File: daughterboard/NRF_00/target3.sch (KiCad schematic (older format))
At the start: 0 parts

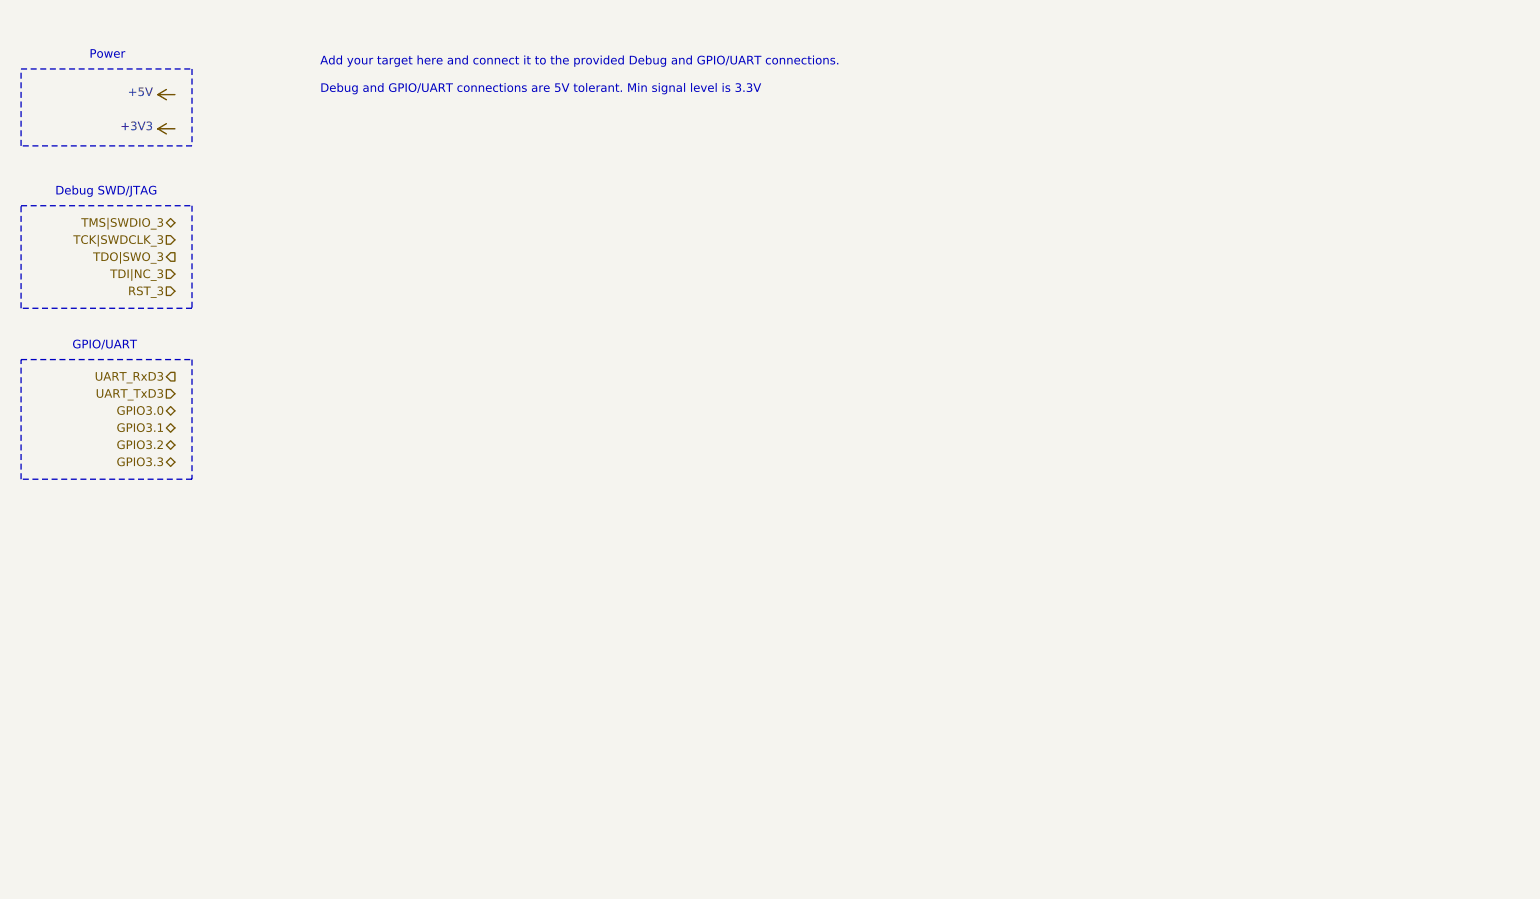
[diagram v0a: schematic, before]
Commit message: finished NRF daughterboard schematics
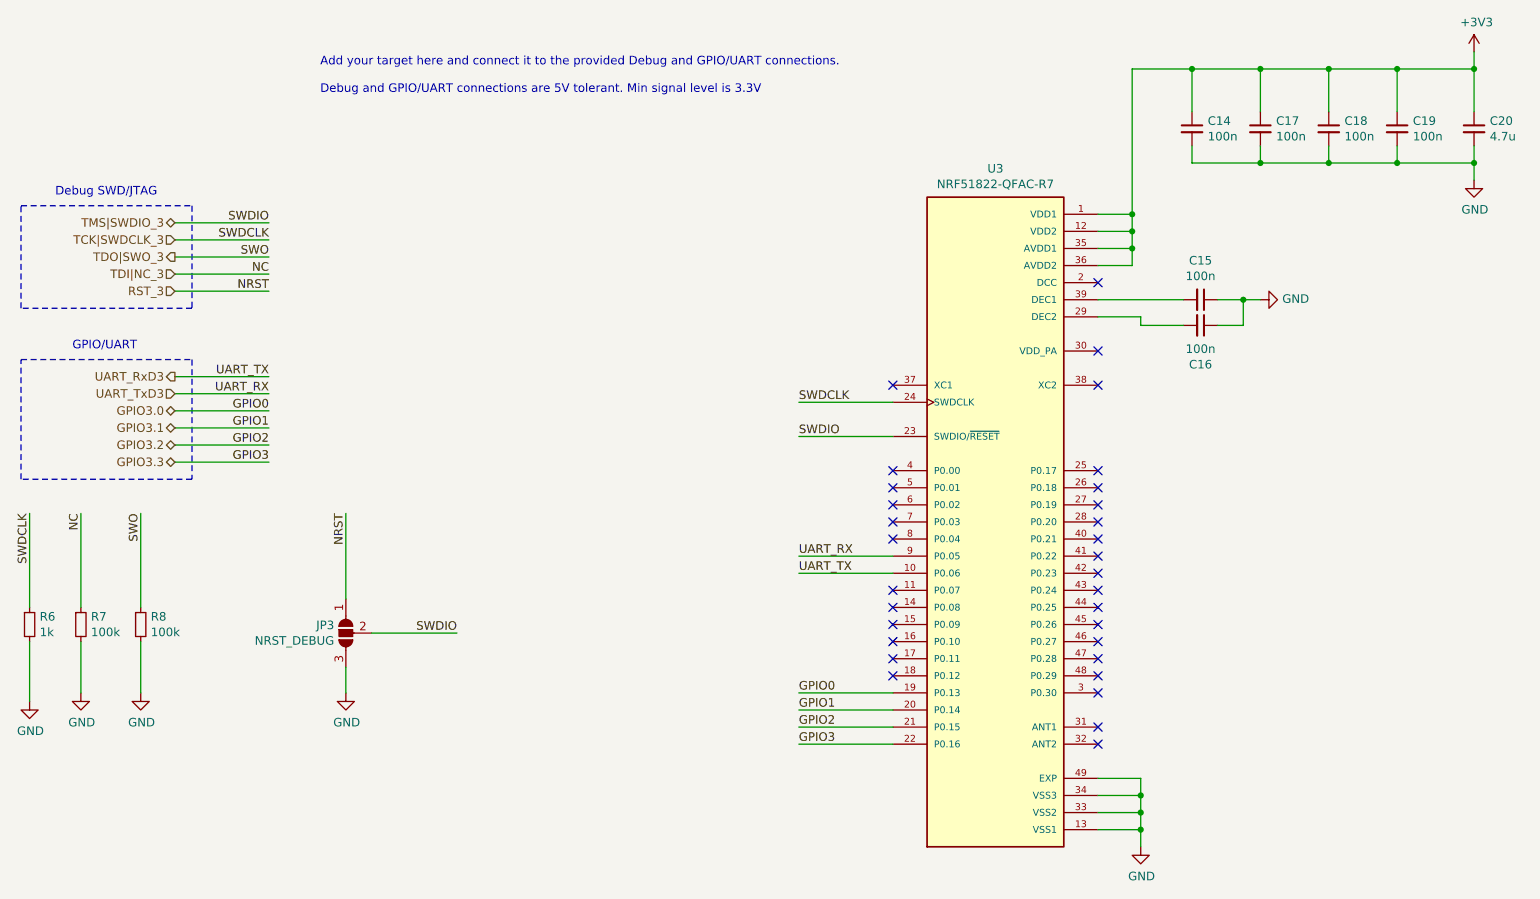
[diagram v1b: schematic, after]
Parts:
- added C14, C15, C16, C17, C18, C19: 100n, symbol Device:C_Small
- added C20: 4.7u, symbol Device:C_Small
- added JP3: NRST_DEBUG, symbol Jumper:SolderJumper_3_Open
- added R6: 1k, symbol Device:R_Small
- added R7, R8: 100k, symbol Device:R_Small
- added U3: NRF51822-QFAC-R7, hive_daughterboard:NRF51822-QFAC-R7, symbol hive_daughterboard:NRF51822-QFAC-R7
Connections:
- net +3V3: now also C14.1, C17.1, C18.1, C19.1, C20.1, U3.1 (VDD1), U3.12 (VDD2), U3.35 (AVDD1), U3.36 (AVDD2)
- net GPIO3.0: now also U3.19 (P0.13)
- net GPIO3.1: now also U3.20 (P0.14)
- net GPIO3.2: now also U3.21 (P0.15)
- net GPIO3.3: now also U3.22 (P0.16)
- net RST_3: now also JP3.1 (A)
- net TCK|SWDCLK_3: now also R6.1, U3.24 (SWDCLK)
- net TDI|NC_3: now also R7.1
- net TDO|SWO_3: now also R8.1
- net TMS|SWDIO_3: now also JP3.2 (C), U3.23 (SWDIO/~RESET)
- net UART_RxD3: now also U3.10 (P0.06)
- net UART_TxD3: now also U3.9 (P0.05)
- new net: C16.2, U3.29 (DEC2)
- new net: C15.2, U3.39 (DEC1)
- new net GND: C14.2, C15.1, C16.1, C17.2, C18.2, C19.2, C20.2, JP3.3 (B), R6.2, R7.2, R8.2, U3.13 (VSS1), U3.33 (VSS2), U3.34 (VSS3), U3.49 (EXP)
- no-connect marks 0 -> 31
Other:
- note removed: "Power"

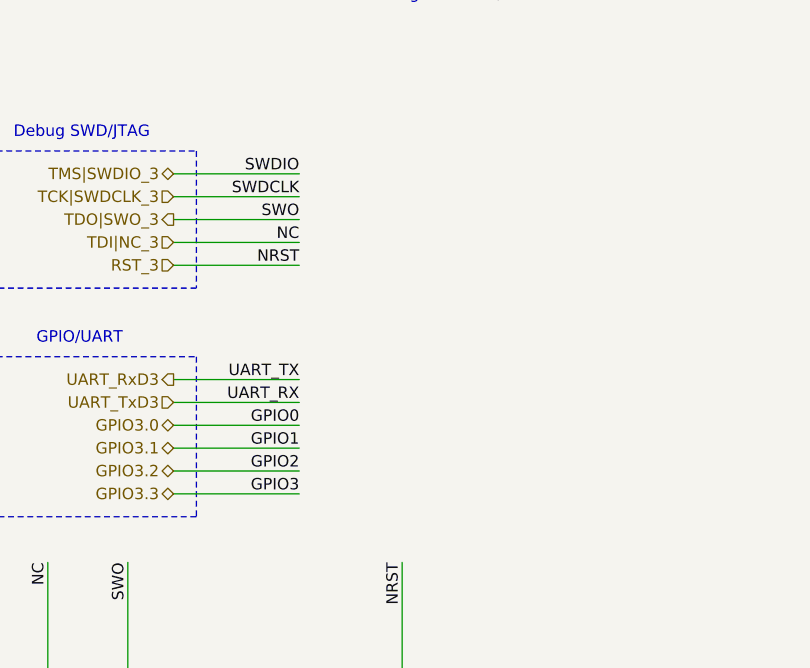
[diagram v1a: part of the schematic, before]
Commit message: added testpoints to daughterboards, updated readme
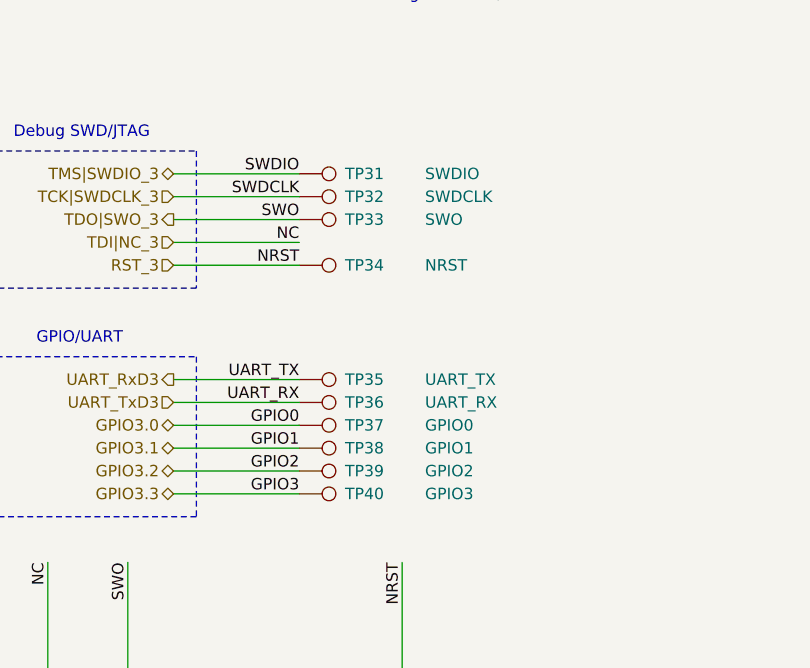
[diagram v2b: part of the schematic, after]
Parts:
- added TP31: SWDIO, symbol Connector:TestPoint
- added TP32: SWDCLK, symbol Connector:TestPoint
- added TP33: SWO, symbol Connector:TestPoint
- added TP34: NRST, symbol Connector:TestPoint
- added TP35: UART_TX, symbol Connector:TestPoint
- added TP36: UART_RX, symbol Connector:TestPoint
- added TP37: GPIO0, symbol Connector:TestPoint
- added TP38: GPIO1, symbol Connector:TestPoint
- added TP39: GPIO2, symbol Connector:TestPoint
- added TP40: GPIO3, symbol Connector:TestPoint
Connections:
- net GPIO3.0: now also TP37.1
- net GPIO3.1: now also TP38.1
- net GPIO3.2: now also TP39.1
- net GPIO3.3: now also TP40.1
- net RST_3: now also TP34.1
- net TCK|SWDCLK_3: now also TP32.1
- net TDO|SWO_3: now also TP33.1
- net TMS|SWDIO_3: now also TP31.1
- net UART_RxD3: now also TP35.1
- net UART_TxD3: now also TP36.1
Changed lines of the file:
@@
 	7300 5350 7300 5250
 Connection ~ 7300 5250
+$Comp
+L Connector:TestPoint TP?
+U 1 1 61914E59
+P 2200 2100
+AR Path="/616688D6/61914E59" Ref="TP?"  Part="1"
+AR Path="/61668157/61914E59" Ref="TP34"  Part="1"
+F 0 "TP34" V 2200 2300 50  0000 L CNN
+F 1 "NRST" V 2200 2650 50  0000 L CNN
+F 2 "" H 2400 2100 50  0001 C CNN
+F 3 "~" H 2400 2100 50  0001 C CNN
+	1    2200 2100
+	0    1    1    0
+$EndComp
+$Comp
+L Connector:TestPoint TP?
+U 1 1 61914E5F
+P 2200 1900
+AR Path="/616688D6/61914E5F" Ref="TP?"  Part="1"
+AR Path="/61668157/61914E5F" Ref="TP33"  Part="1"
+F 0 "TP33" V 2200 2100 50  0000 L CNN
+F 1 "SWO" V 2200 2450 50  0000 L CNN
+F 2 "" H 2400 1900 50  0001 C CNN
+F 3 "~" H 2400 1900 50  0001 C CNN
+	1    2200 1900
+	0    1    1    0
+$EndComp
+$Comp
+L Connector:TestPoint TP?
+U 1 1 61914E65
+P 2200 1800
+AR Path="/616688D6/61914E65" Ref="TP?"  Part="1"
+AR Path="/61668157/61914E65" Ref="TP32"  Part="1"
+F 0 "TP32" V 2200 2000 50  0000 L CNN
+F 1 "SWDCLK" V 2200 2350 50  0000 L CNN
+F 2 "" H 2400 1800 50  0001 C CNN
+F 3 "~" H 2400 1800 50  0001 C CNN
+	1    2200 1800
+	0    1    1    0
+$EndComp
+$Comp
+L Connector:TestPoint TP?
+U 1 1 61914E6B
+P 2200 1700
+AR Path="/616688D6/61914E6B" Ref="TP?"  Part="1"
+AR Path="/61668157/61914E6B" Ref="TP31"  Part="1"
+F 0 "TP31" V 2200 1900 50  0000 L CNN
+F 1 "SWDIO" V 2200 2250 50  0000 L CNN
+F 2 "" H 2400 1700 50  0001 C CNN
+F 3 "~" H 2400 1700 50  0001 C CNN
+	1    2200 1700
+	0    1    1    0
+$EndComp
+$Comp
+L Connector:TestPoint TP?
+U 1 1 61914E71
+P 2200 2600
+AR Path="/616688D6/61914E71" Ref="TP?"  Part="1"
+AR Path="/61668157/61914E71" Ref="TP35"  Part="1"
+F 0 "TP35" V 2200 2800 50  0000 L CNN
+F 1 "UART_TX" V 2200 3150 50  0000 L CNN
+F 2 "" H 2400 2600 50  0001 C CNN
+F 3 "~" H 2400 2600 50  0001 C CNN
+	1    2200 2600
+	0    1    1    0
+$EndComp
+$Comp
+L Connector:TestPoint TP?
+U 1 1 61914E77
+P 2200 2700
+AR Path="/616688D6/61914E77" Ref="TP?"  Part="1"
+AR Path="/61668157/61914E77" Ref="TP36"  Part="1"
+F 0 "TP36" V 2200 2900 50  0000 L CNN
+F 1 "UART_RX" V 2200 3250 50  0000 L CNN
+F 2 "" H 2400 2700 50  0001 C CNN
+F 3 "~" H 2400 2700 50  0001 C CNN
+	1    2200 2700
+	0    1    1    0
+$EndComp
+$Comp
+L Connector:TestPoint TP?
+U 1 1 61914E7D
+P 2200 2800
+AR Path="/616688D6/61914E7D" Ref="TP?"  Part="1"
+AR Path="/61668157/61914E7D" Ref="TP37"  Part="1"
+F 0 "TP37" V 2200 3000 50  0000 L CNN
+F 1 "GPIO0" V 2200 3350 50  0000 L CNN
+F 2 "" H 2400 2800 50  0001 C CNN
+F 3 "~" H 2400 2800 50  0001 C CNN
+	1    2200 2800
+	0    1    1    0
+$EndComp
+$Comp
+L Connector:TestPoint TP?
+U 1 1 61914E83
+P 2200 2900
+AR Path="/616688D6/61914E83" Ref="TP?"  Part="1"
+AR Path="/61668157/61914E83" Ref="TP38"  Part="1"
+F 0 "TP38" V 2200 3100 50  0000 L CNN
+F 1 "GPIO1" V 2200 3450 50  0000 L CNN
+F 2 "" H 2400 2900 50  0001 C CNN
+F 3 "~" H 2400 2900 50  0001 C CNN
+	1    2200 2900
+	0    1    1    0
+$EndComp
+$Comp
+L Connector:TestPoint TP?
+U 1 1 61914E89
+P 2200 3000
+AR Path="/616688D6/61914E89" Ref="TP?"  Part="1"
+AR Path="/61668157/61914E89" Ref="TP39"  Part="1"
+F 0 "TP39" V 2200 3200 50  0000 L CNN
+F 1 "GPIO2" V 2200 3550 50  0000 L CNN
+F 2 "" H 2400 3000 50  0001 C CNN
+F 3 "~" H 2400 3000 50  0001 C CNN
+	1    2200 3000
+	0    1    1    0
+$EndComp
+$Comp
+L Connector:TestPoint TP?
+U 1 1 61914E8F
+P 2200 3100
+AR Path="/616688D6/61914E8F" Ref="TP?"  Part="1"
+AR Path="/61668157/61914E8F" Ref="TP40"  Part="1"
+F 0 "TP40" V 2200 3300 50  0000 L CNN
+F 1 "GPIO3" V 2200 3650 50  0000 L CNN
+F 2 "" H 2400 3100 50  0001 C CNN
+F 3 "~" H 2400 3100 50  0001 C CNN
+	1    2200 3100
+	0    1    1    0
+$EndComp
 $EndSCHEMATC

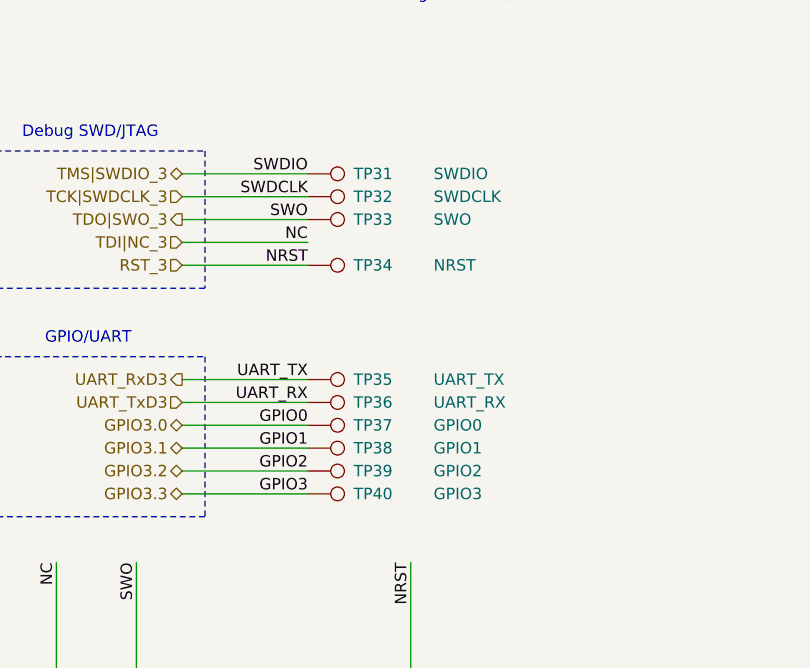
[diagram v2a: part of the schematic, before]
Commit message: finished NRF daughterboard layout
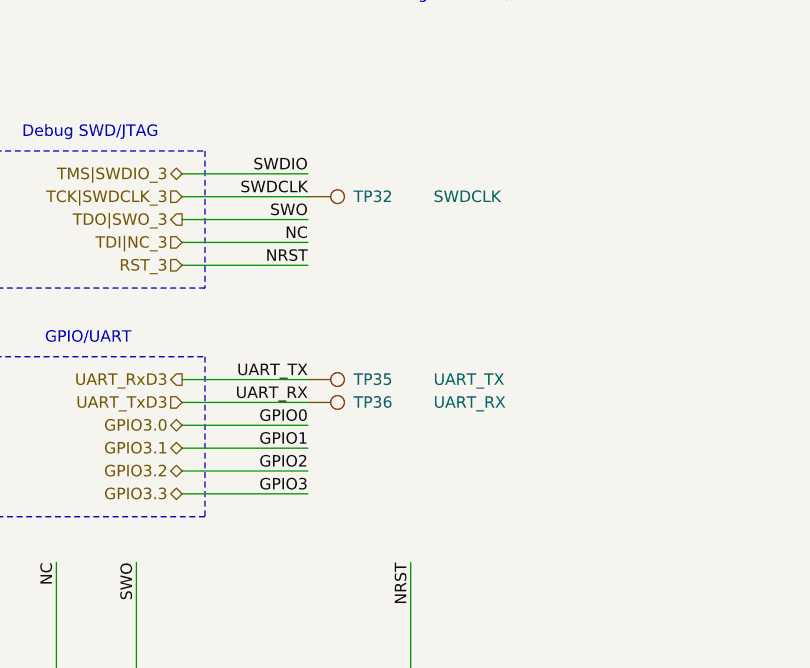
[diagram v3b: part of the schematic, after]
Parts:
- removed TP31: SWDIO, symbol Connector:TestPoint
- removed TP33: SWO, symbol Connector:TestPoint
- removed TP34: NRST, symbol Connector:TestPoint
- removed TP37: GPIO0, symbol Connector:TestPoint
- removed TP38: GPIO1, symbol Connector:TestPoint
- removed TP39: GPIO2, symbol Connector:TestPoint
- removed TP40: GPIO3, symbol Connector:TestPoint
- C14, C15, C16, C17, C18, C19, C20: footprint (none) -> Capacitor_SMD:C_0603_1608Metric_Pad1.05x0.95mm_HandSolder
- JP3: footprint (none) -> Jumper:SolderJumper-3_P2.0mm_Open_TrianglePad1.0x1.5mm_NumberLabels
- R6, R7, R8: footprint (none) -> Resistor_SMD:R_0603_1608Metric_Pad1.05x0.95mm_HandSolder
- TP32, TP35, TP36: footprint (none) -> TestPoint:TestPoint_Pad_1.0x1.0mm
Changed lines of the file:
@@
 F 0 "R7" H 1159 4096 50  0000 L CNN
 F 1 "100k" H 1159 4005 50  0000 L CNN
-F 2 "" H 1100 4050 50  0001 C CNN
+F 2 "Resistor_SMD:R_0603_1608Metric_Pad1.05x0.95mm_HandSolder" H 1100 4050 50  0001 C CNN
 F 3 "~" H 1100 4050 50  0001 C CNN
 	1    1100 4050
@@
 F 0 "R6" H 859 4096 50  0000 L CNN
 F 1 "1k" H 859 4005 50  0000 L CNN
-F 2 "" H 800 4050 50  0001 C CNN
+F 2 "Resistor_SMD:R_0603_1608Metric_Pad1.05x0.95mm_HandSolder" H 800 4050 50  0001 C CNN
 F 3 "~" H 800 4050 50  0001 C CNN
 	1    800  4050
@@
 F 0 "JP3" V 2604 4168 50  0000 L CNN
 F 1 "NRST_DEBUG" V 2695 4168 50  0000 L CNN
-F 2 "" H 2650 4100 50  0001 C CNN
+F 2 "Jumper:SolderJumper-3_P2.0mm_Open_TrianglePad1.0x1.5mm_NumberLabels" H 2650 4100 50  0001 C CNN
 F 3 "~" H 2650 4100 50  0001 C CNN
 	1    2650 4100
@@
 F 0 "C14" H 7692 1196 50  0000 L CNN
 F 1 "100n" H 7692 1105 50  0000 L CNN
-F 2 "" H 7600 1150 50  0001 C CNN
+F 2 "Capacitor_SMD:C_0603_1608Metric_Pad1.05x0.95mm_HandSolder" H 7600 1150 50  0001 C CNN
 F 3 "~" H 7600 1150 50  0001 C CNN
 	1    7600 1150
@@
 F 0 "C17" H 8092 1196 50  0000 L CNN
 F 1 "100n" H 8092 1105 50  0000 L CNN
-F 2 "" H 8000 1150 50  0001 C CNN
+F 2 "Capacitor_SMD:C_0603_1608Metric_Pad1.05x0.95mm_HandSolder" H 8000 1150 50  0001 C CNN
 F 3 "~" H 8000 1150 50  0001 C CNN
 	1    8000 1150
@@
 F 0 "C18" H 8492 1196 50  0000 L CNN
 F 1 "100n" H 8492 1105 50  0000 L CNN
-F 2 "" H 8400 1150 50  0001 C CNN
+F 2 "Capacitor_SMD:C_0603_1608Metric_Pad1.05x0.95mm_HandSolder" H 8400 1150 50  0001 C CNN
 F 3 "~" H 8400 1150 50  0001 C CNN
 	1    8400 1150
@@
 F 0 "C19" H 8892 1196 50  0000 L CNN
 F 1 "100n" H 8892 1105 50  0000 L CNN
-F 2 "" H 8800 1150 50  0001 C CNN
+F 2 "Capacitor_SMD:C_0603_1608Metric_Pad1.05x0.95mm_HandSolder" H 8800 1150 50  0001 C CNN
 F 3 "~" H 8800 1150 50  0001 C CNN
 	1    8800 1150
@@
 F 0 "C20" H 9342 1196 50  0000 L CNN
 F 1 "4.7u" H 9342 1105 50  0000 L CNN
-F 2 "" H 9250 1150 50  0001 C CNN
+F 2 "Capacitor_SMD:C_0603_1608Metric_Pad1.05x0.95mm_HandSolder" H 9250 1150 50  0001 C CNN
 F 3 "~" H 9250 1150 50  0001 C CNN
 	1    9250 1150
@@
 F 0 "C15" V 7421 2150 50  0000 C CNN
 F 1 "100n" V 7512 2150 50  0000 C CNN
-F 2 "" H 7650 2150 50  0001 C CNN
+F 2 "Capacitor_SMD:C_0603_1608Metric_Pad1.05x0.95mm_HandSolder" H 7650 2150 50  0001 C CNN
 F 3 "~" H 7650 2150 50  0001 C CNN
 	1    7650 2150
@@
 F 0 "C16" V 7421 2300 50  0000 C CNN
 F 1 "100n" V 7512 2300 50  0000 C CNN
-F 2 "" H 7650 2300 50  0001 C CNN
+F 2 "Capacitor_SMD:C_0603_1608Metric_Pad1.05x0.95mm_HandSolder" H 7650 2300 50  0001 C CNN
 F 3 "~" H 7650 2300 50  0001 C CNN
 	1    7650 2300
@@
 F 0 "R8" H 1509 4096 50  0000 L CNN
 F 1 "100k" H 1509 4005 50  0000 L CNN
-F 2 "" H 1450 4050 50  0001 C CNN
+F 2 "Resistor_SMD:R_0603_1608Metric_Pad1.05x0.95mm_HandSolder" H 1450 4050 50  0001 C CNN
 F 3 "~" H 1450 4050 50  0001 C CNN
 	1    1450 4050
@@
 $Comp
 L Connector:TestPoint TP?
-U 1 1 61914E59
-P 2200 2100
-AR Path="/616688D6/61914E59" Ref="TP?"  Part="1"
-AR Path="/61668157/61914E59" Ref="TP34"  Part="1"
-F 0 "TP34" V 2200 2300 50  0000 L CNN
-F 1 "NRST" V 2200 2650 50  0000 L CNN
-F 2 "" H 2400 2100 50  0001 C CNN
-F 3 "~" H 2400 2100 50  0001 C CNN
-	1    2200 2100
-	0    1    1    0
-$EndComp
-$Comp
-L Connector:TestPoint TP?
-U 1 1 61914E5F
-P 2200 1900
-AR Path="/616688D6/61914E5F" Ref="TP?"  Part="1"
-AR Path="/61668157/61914E5F" Ref="TP33"  Part="1"
-F 0 "TP33" V 2200 2100 50  0000 L CNN
-F 1 "SWO" V 2200 2450 50  0000 L CNN
-F 2 "" H 2400 1900 50  0001 C CNN
-F 3 "~" H 2400 1900 50  0001 C CNN
-	1    2200 1900
-	0    1    1    0
-$EndComp
-$Comp
-L Connector:TestPoint TP?
 U 1 1 61914E65
 P 2200 1800
@@
 F 0 "TP32" V 2200 2000 50  0000 L CNN
 F 1 "SWDCLK" V 2200 2350 50  0000 L CNN
-F 2 "" H 2400 1800 50  0001 C CNN
+F 2 "TestPoint:TestPoint_Pad_1.0x1.0mm" H 2400 1800 50  0001 C CNN
 F 3 "~" H 2400 1800 50  0001 C CNN
 	1    2200 1800
-	0    1    1    0
-$EndComp
-$Comp
-L Connector:TestPoint TP?
-U 1 1 61914E6B
-P 2200 1700
-AR Path="/616688D6/61914E6B" Ref="TP?"  Part="1"
-AR Path="/61668157/61914E6B" Ref="TP31"  Part="1"
-F 0 "TP31" V 2200 1900 50  0000 L CNN
-F 1 "SWDIO" V 2200 2250 50  0000 L CNN
-F 2 "" H 2400 1700 50  0001 C CNN
-F 3 "~" H 2400 1700 50  0001 C CNN
-	1    2200 1700
 	0    1    1    0
 $EndComp
@@
 F 0 "TP35" V 2200 2800 50  0000 L CNN
 F 1 "UART_TX" V 2200 3150 50  0000 L CNN
-F 2 "" H 2400 2600 50  0001 C CNN
+F 2 "TestPoint:TestPoint_Pad_1.0x1.0mm" H 2400 2600 50  0001 C CNN
 F 3 "~" H 2400 2600 50  0001 C CNN
 	1    2200 2600
@@
 F 0 "TP36" V 2200 2900 50  0000 L CNN
 F 1 "UART_RX" V 2200 3250 50  0000 L CNN
-F 2 "" H 2400 2700 50  0001 C CNN
+F 2 "TestPoint:TestPoint_Pad_1.0x1.0mm" H 2400 2700 50  0001 C CNN
 F 3 "~" H 2400 2700 50  0001 C CNN
 	1    2200 2700
 	0    1    1    0
 $EndComp
-$Comp
-L Connector:TestPoint TP?
-U 1 1 61914E7D
-P 2200 2800
-AR Path="/616688D6/61914E7D" Ref="TP?"  Part="1"
-AR Path="/61668157/61914E7D" Ref="TP37"  Part="1"
-F 0 "TP37" V 2200 3000 50  0000 L CNN
-F 1 "GPIO0" V 2200 3350 50  0000 L CNN
-F 2 "" H 2400 2800 50  0001 C CNN
-F 3 "~" H 2400 2800 50  0001 C CNN
-	1    2200 2800
-	0    1    1    0
-$EndComp
-$Comp
-L Connector:TestPoint TP?
-U 1 1 61914E83
-P 2200 2900
-AR Path="/616688D6/61914E83" Ref="TP?"  Part="1"
-AR Path="/61668157/61914E83" Ref="TP38"  Part="1"
-F 0 "TP38" V 2200 3100 50  0000 L CNN
-F 1 "GPIO1" V 2200 3450 50  0000 L CNN
-F 2 "" H 2400 2900 50  0001 C CNN
-F 3 "~" H 2400 2900 50  0001 C CNN
-	1    2200 2900
-	0    1    1    0
-$EndComp
-$Comp
-L Connector:TestPoint TP?
-U 1 1 61914E89
-P 2200 3000
-AR Path="/616688D6/61914E89" Ref="TP?"  Part="1"
-AR Path="/61668157/61914E89" Ref="TP39"  Part="1"
-F 0 "TP39" V 2200 3200 50  0000 L CNN
-F 1 "GPIO2" V 2200 3550 50  0000 L CNN
-F 2 "" H 2400 3000 50  0001 C CNN
-F 3 "~" H 2400 3000 50  0001 C CNN
-	1    2200 3000
-	0    1    1    0
-$EndComp
-$Comp
-L Connector:TestPoint TP?
-U 1 1 61914E8F
-P 2200 3100
-AR Path="/616688D6/61914E8F" Ref="TP?"  Part="1"
-AR Path="/61668157/61914E8F" Ref="TP40"  Part="1"
-F 0 "TP40" V 2200 3300 50  0000 L CNN
-F 1 "GPIO3" V 2200 3650 50  0000 L CNN
-F 2 "" H 2400 3100 50  0001 C CNN
-F 3 "~" H 2400 3100 50  0001 C CNN
-	1    2200 3100
-	0    1    1    0
-$EndComp
